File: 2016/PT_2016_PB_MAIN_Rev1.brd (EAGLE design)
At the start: 150.9 x 201.9 mm, 137 parts, among them M1+ ANDERSON_POWERPOLEPP45_PCB_HO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, M1- ANDERSON_POWERPOLEPP45_PCB_HO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, M2+ ANDERSON_POWERPOLEPP45_PCB_HO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, M2- ANDERSON_POWERPOLEPP45_PCB_HO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, M3+ ANDERSON_POWERPOLEPP45_PCB_HO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, M3- ANDERSON_POWERPOLEPP45_PCB_HO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, M4+ ANDERSON_POWERPOLEPP45_PCB_HO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, M4- ANDERSON_POWERPOLEPP45_PCB_HO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, M5+ ANDERSON_POWERPOLEPP45_PCB_HO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, M5- ANDERSON_POWERPOLEPP45_PCB_HO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

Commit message: New Layout Idea
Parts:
- removed U$45: APP_2POS_CONFIG5V_VERT, MRDT-Connectors:APP45_5V_VERT_CONFIG
- removed U$46: APP_2POS_CONFIG12V_VERT, MRDT-Connectors:APP45_12V_VERT_CONFIG
- added M2-1, M2-2, M2-3, M2-4: ANDERSON_POWERPOLEPP45_PCB_HORIZ_RIGHT, MRDT-Connectors:APP45_PCB_HORIZ_RIGHT
- added U$25: APP_MOUTING_WINGHORIZ, MRDT-Connectors:APP45_MOUNTING_WING_HORIZ
- moved R8 194.5 mm to (17.5, 162.3), turned to 270 degrees
- moved LED3 187.4 mm to (17.5, 157.2), turned to 270 degrees
- moved 5V-INT 174.2 mm to (137.0, 18.9)
- moved LED5 174.2 mm to (142.6, 13.3)
- moved R13 174.2 mm to (137.7, 13.6)
- moved C12 171.4 mm to (30.5, 157.2), flipped to the top, turned to 180 degrees
- moved U$3 168.7 mm to (33.0, 163.3), flipped to the top
- moved R10 167.1 mm to (17.5, 146.1), turned to 270 degrees
- moved C11 167.0 mm to (35.6, 157.2), flipped to the top, turned to 180 degrees
- moved LED2 159.9 mm to (17.5, 141.0), turned to 270 degrees
- moved U$21 136.5 mm to (33.0, 147.6), turned to 180 degrees
- moved C43 133.5 mm to (30.5, 141.7)
- moved R1 126.7 mm to (126.2, 43.7), flipped to the bottom, turned to 90 degrees
- moved R2 126.0 mm to (126.0, 27.4), flipped to the bottom, turned to 90 degrees
- moved C6 125.5 mm to (35.6, 141.7)
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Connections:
- net 12V-AUX: now also M2-2.P$1; no longer U$46.VCC
- net 12V-SIG: now also U$4.PN3; no longer U$4.PP2
- net 5V-AUX: now also M2-4.P$1; no longer U$45.VCC
- net 5V-SIG: now also U$4.PP2; no longer U$4.PN3
- net GND: now also M2-1.P$1, M2-3.P$1; no longer U$45.GND, U$46.GND
- net RX1: now also U$24.RO; no longer U$12.RO
- net RX2: now also U$12.RO; no longer U$24.RO
- net TX1: now also U$24.DI; no longer U$12.DI
- net TX2: now also U$12.DI; no longer U$24.DI
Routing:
- net N$33: track 12.3 -> 190.0 mm
- net TX1: track 41.8 -> 179.7 mm, vias 0 -> 1
- net RX1: track 39.0 -> 170.8 mm, vias 0 -> 1
- net N$7: track 0.00 -> 120.9 mm
- net RX2: track 116.7 -> 227.1 mm, vias 2 -> 1
- net TX2: track 119.9 -> 220.8 mm, vias 2 -> 1
- net 5V-IMEAS: track 182.3 -> 113.8 mm
- net M2-SIG: track 225.4 -> 258.0 mm, vias 0 -> 1
- net M1-SIG: track 246.7 -> 279.1 mm, vias 0 -> 1
- net M4-SIG: track 183.5 -> 215.6 mm, vias 0 -> 1
- net M5-SIG: track 167.8 -> 199.8 mm, vias 0 -> 1
- net M3-SIG: track 198.4 -> 230.4 mm, vias 0 -> 1
- net AUX_P-SIG: track 122.7 -> 154.7 mm, vias 0 -> 1
- net M6-SIG: track 145.5 -> 177.5 mm, vias 0 -> 1
- net AUX_P2-SIG: track 92.6 -> 124.6 mm, vias 0 -> 1
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- added copper zone on layer 1, net 5V-AUX
- added copper zone on layer 1, net N$7
- removed copper zone on layer 16, net 5V-AUX
- removed copper zone on layer 1, net GND
- removed copper zone on layer 16, net N$7

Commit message: Routed new layout
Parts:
- added U$26, U$27, U$28, U$29: ANDERSON_POWERPOLEPP45_PCB_HORIZ_RIGHT_2HIGH, MRDT-Connectors:APP45_PCB_HORIZ_RIGHT_2HIGH
- added X1: 22-23-2041, con-molex:22-23-2041
- moved M2-1 15.7 mm to (-16.3, 154.2)
- moved M2-4 15.7 mm to (-16.3, 146.3)
- moved M2-2 7.87 mm to (-16.3, 138.4)
- moved M2-3 7.87 mm to (-16.3, 162.1)
- moved LED2 7.73 mm to (11.9, 146.3), turned to 180 degrees
- moved LED3 7.38 mm to (11.9, 162.1), turned to 180 degrees
- moved R8 1.66 mm to (15.9, 162.4)
- moved R10 1.61 mm to (16.0, 146.6)
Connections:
- new net N$11: M2-2.P$1, X1.1
- new net N$3: M2-3.P$1, X1.4
- new net N$5: M2-1.P$1, X1.3
- new net N$8: M2-4.P$1, X1.2
- net 12V-AUX: now also U$26.P$2; no longer M2-2.P$1
- net 5V-AUX: now also U$27.P$2; no longer M2-4.P$1
- net GND: now also U$28.P$2, U$29.P$2; no longer M2-1.P$1, M2-3.P$1
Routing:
- net N$11: track 0.00 -> 65.3 mm, vias 0 -> 2
- net N$8: track 0.00 -> 60.5 mm, vias 0 -> 2
- net N$5: track 0.00 -> 55.5 mm, vias 0 -> 2
- net N$3: track 0.00 -> 41.0 mm, vias 0 -> 2
- net PRIMARY-VMEAS: track 102.5 -> 129.2 mm
- net AUX_P-SIG: track 154.7 -> 168.2 mm
- net M6-SIG: track 177.5 -> 190.9 mm
- net AUX_P2-SIG: track 124.6 -> 138.0 mm
- net M5-SIG: track 199.8 -> 213.2 mm
- net M4-SIG: track 215.6 -> 229.0 mm
- net M3-SIG: track 230.4 -> 243.8 mm
- net M2-SIG: track 258.0 -> 271.1 mm
- net M1-SIG: track 279.1 -> 292.2 mm
- net GND: track 192.9 -> 185.3 mm, vias 31 -> 33
- net N$46: track 2.18 -> 3.04 mm
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
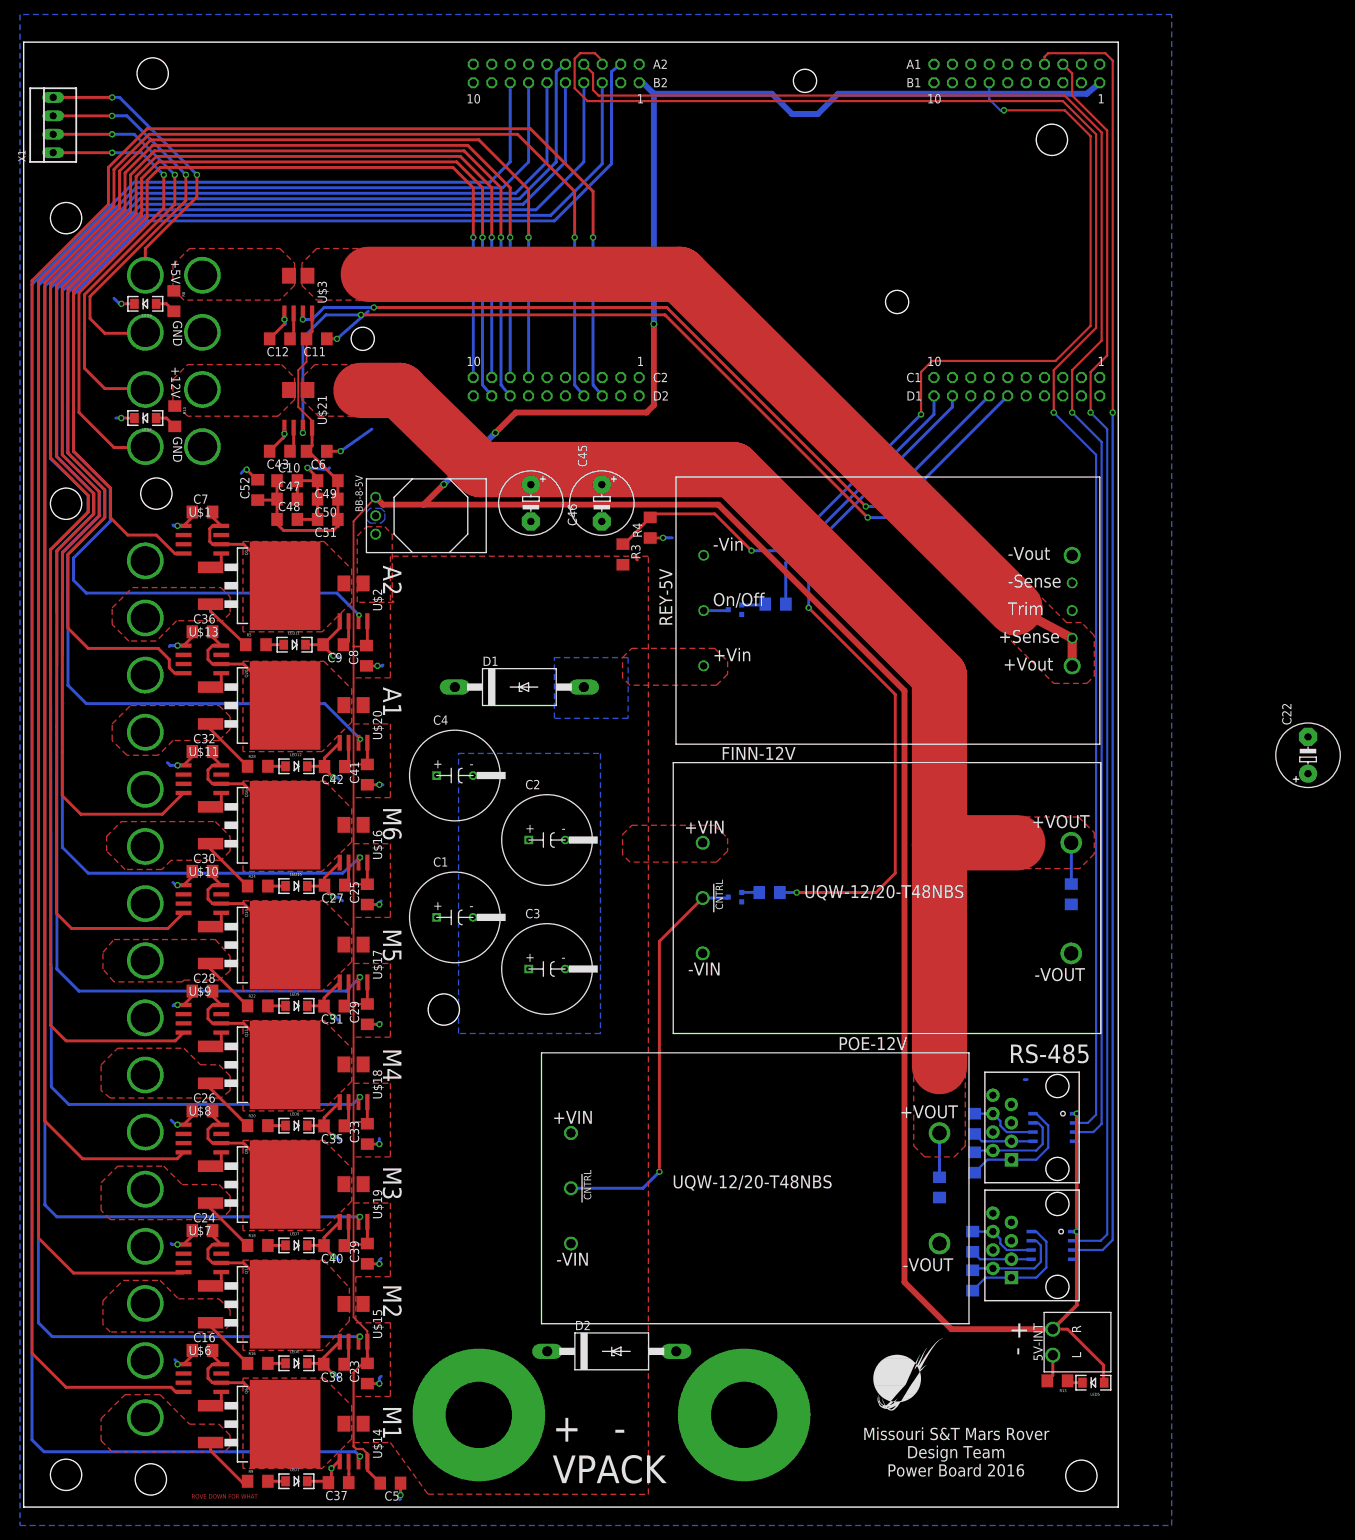
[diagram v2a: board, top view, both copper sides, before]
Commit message: Fixed some clearance issues.
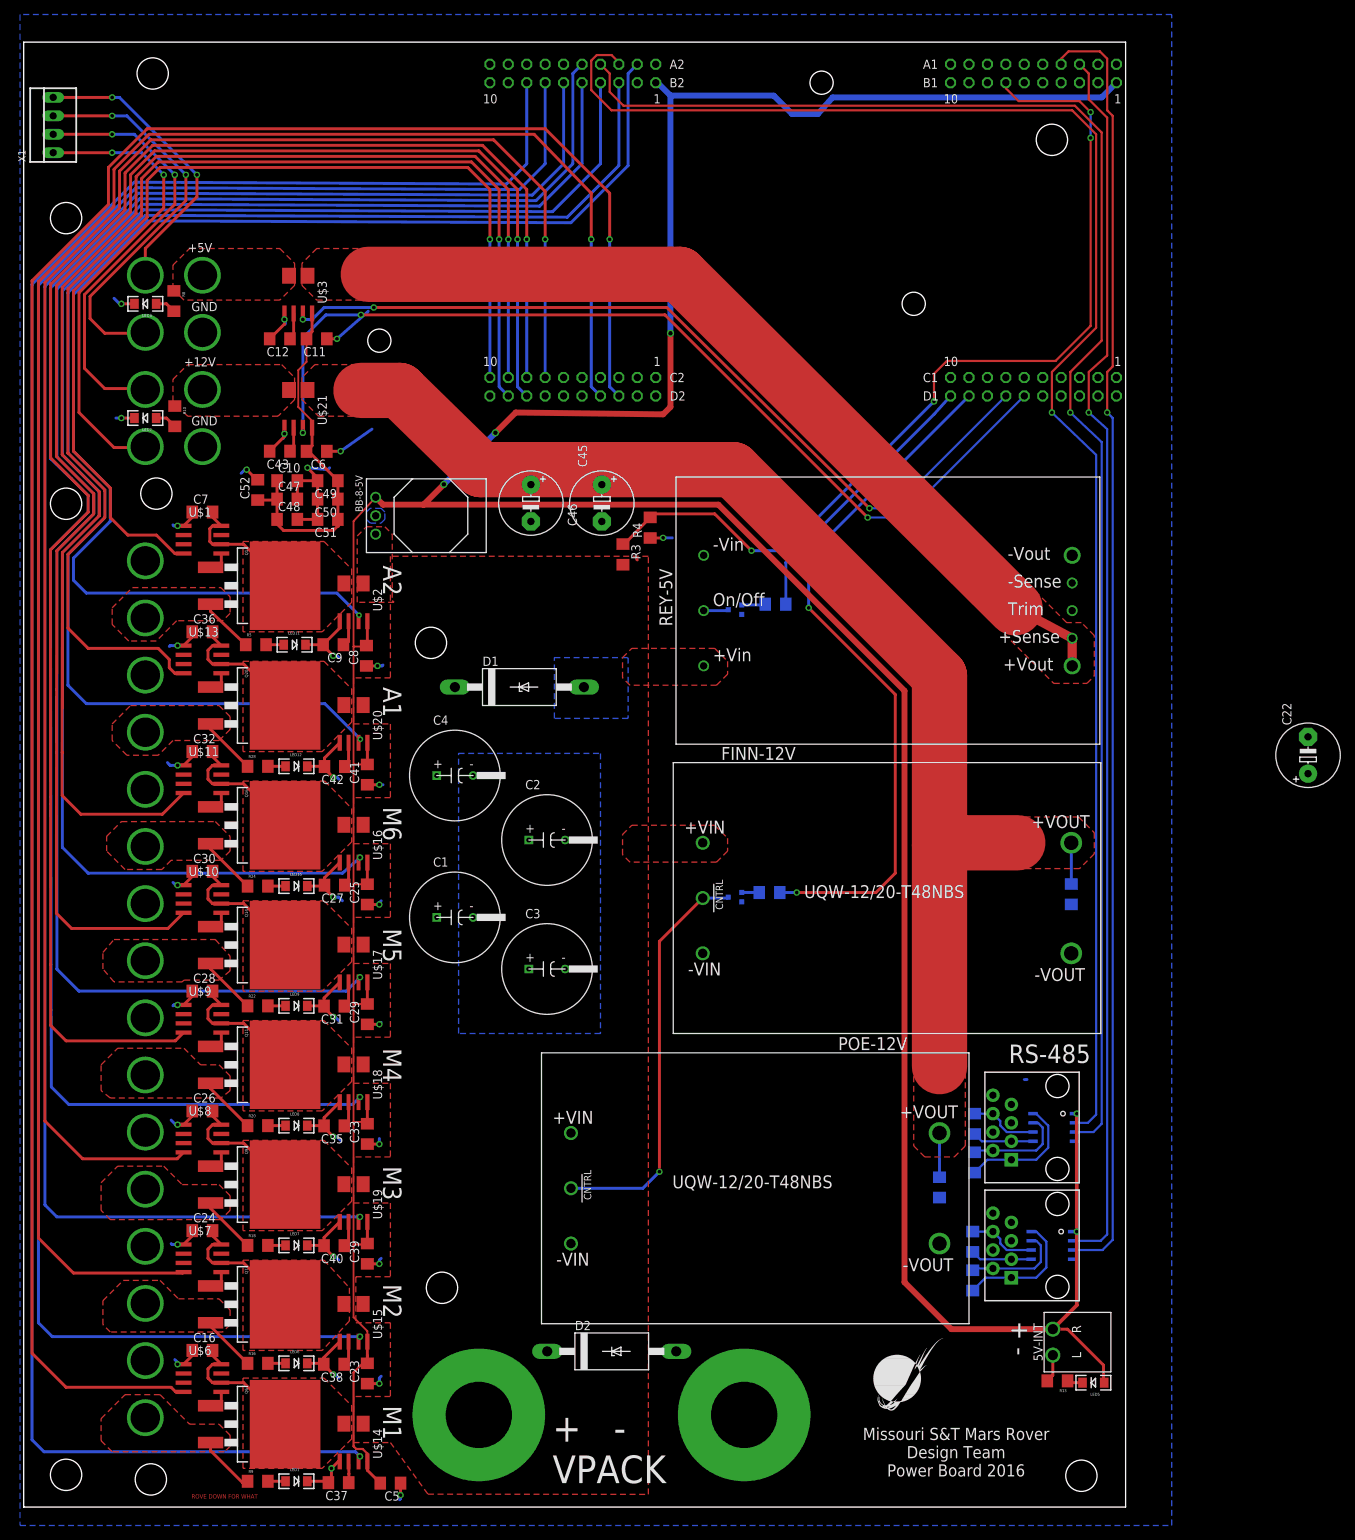
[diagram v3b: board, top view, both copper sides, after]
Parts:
- moved U$4 2.29 mm to (22.6, 140.5)
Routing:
- net M1-IMEAS: track 290.1 -> 292.6 mm
- net M2-IMEAS: track 274.5 -> 277.0 mm
- net M3-IMEAS: track 258.8 -> 261.4 mm
- net M5-IMEAS: track 230.9 -> 233.4 mm
- net M6-IMEAS: track 216.1 -> 218.7 mm
- net AUX_P-IMEAS: track 194.5 -> 197.0 mm
- net M4-IMEAS: track 250.3 -> 252.7 mm
- net AUX_P2-IMEAS: track 181.9 -> 184.3 mm
- net PRIMARY-VMEAS: track 129.2 -> 126.8 mm, vias 3 -> 4
- net 5V-IMEAS: track 113.8 -> 116.2 mm
- net RX2: track 227.1 -> 224.7 mm
- net 12V-IMEAS: track 130.8 -> 133.1 mm
- net M2-SIG: track 271.1 -> 273.4 mm
- net +5V: track 609.7 -> 611.9 mm
- net M5-SIG: track 213.2 -> 215.4 mm
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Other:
- board size 150.9 x 201.9 mm -> 151.9 x 201.9 mm
